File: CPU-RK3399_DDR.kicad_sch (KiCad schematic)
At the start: 29 parts, among them U1 RK3399

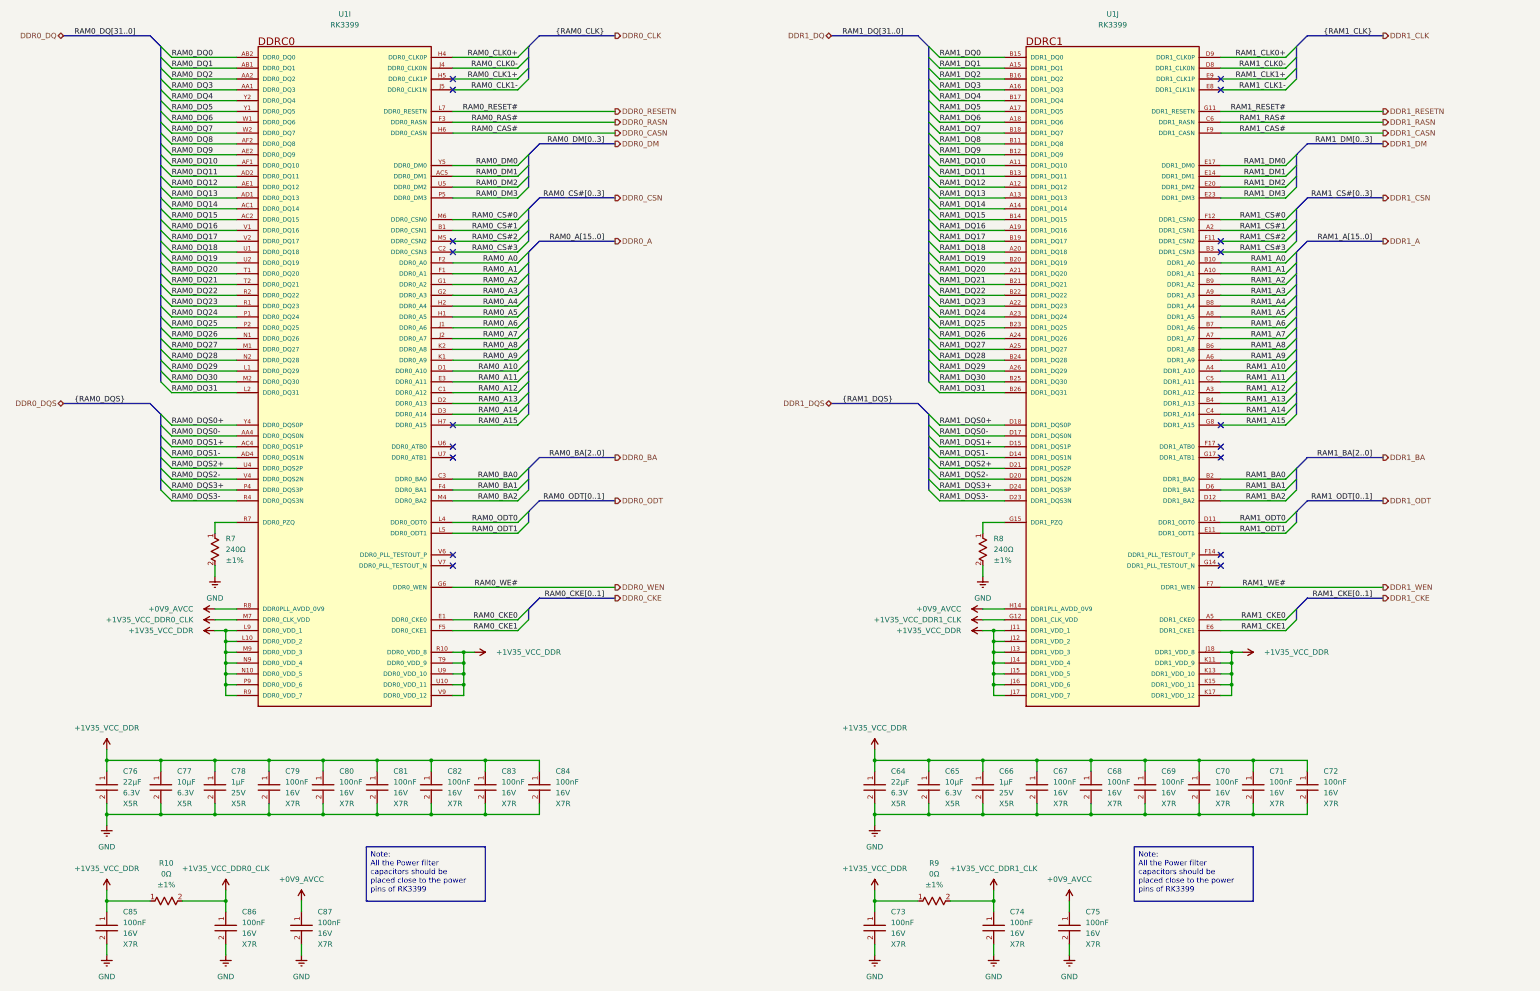
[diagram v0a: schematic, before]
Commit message: design CPU-RK3399 eMMC Controller
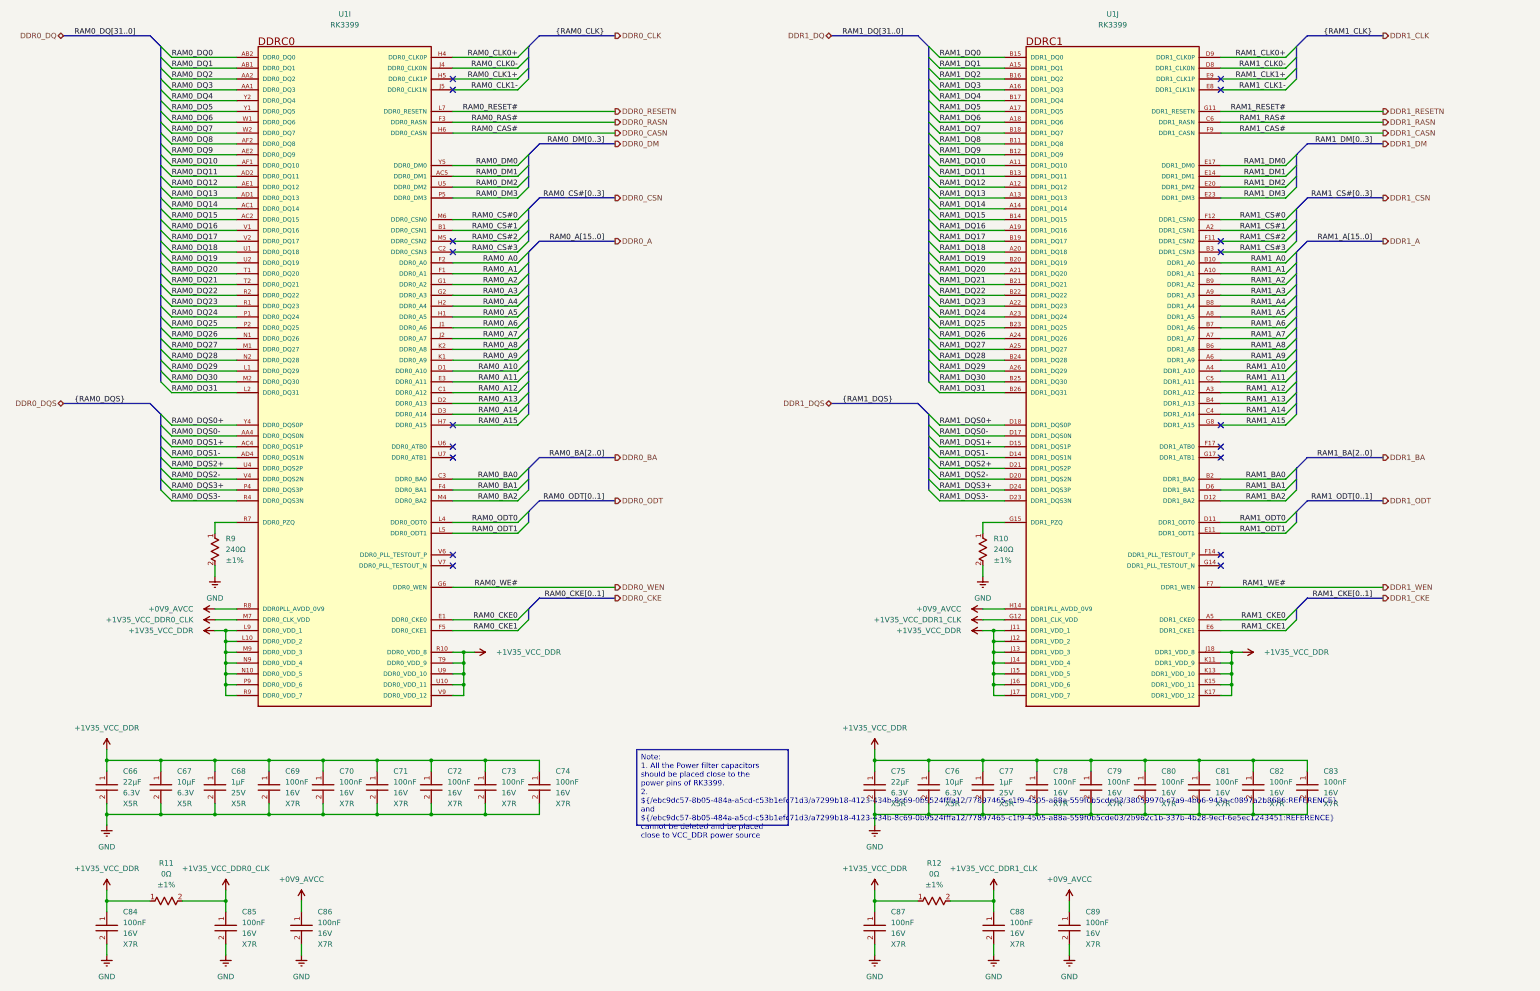
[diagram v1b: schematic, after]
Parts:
- renumbered C76 to C66, C77 to C67, C78 to C68, C79 to C69, C80 to C70, C81 to C71, C82 to C72, C83 to C73, C84 to C74, C64 to C75, C65 to C76, C66 to C77, C67 to C78, C68 to C79, C69 to C80, C70 to C81, C71 to C82, C72 to C83, C85 to C84, C86 to C85, C87 to C86, C73 to C87, C74 to C88, C75 to C89, R8 to R10, R10 to R11, R9 to R12, R7 to R9
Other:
- company: (none) -> TickLab
- title: (none) -> CPU-RK3399 DDR Controller

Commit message: design USB
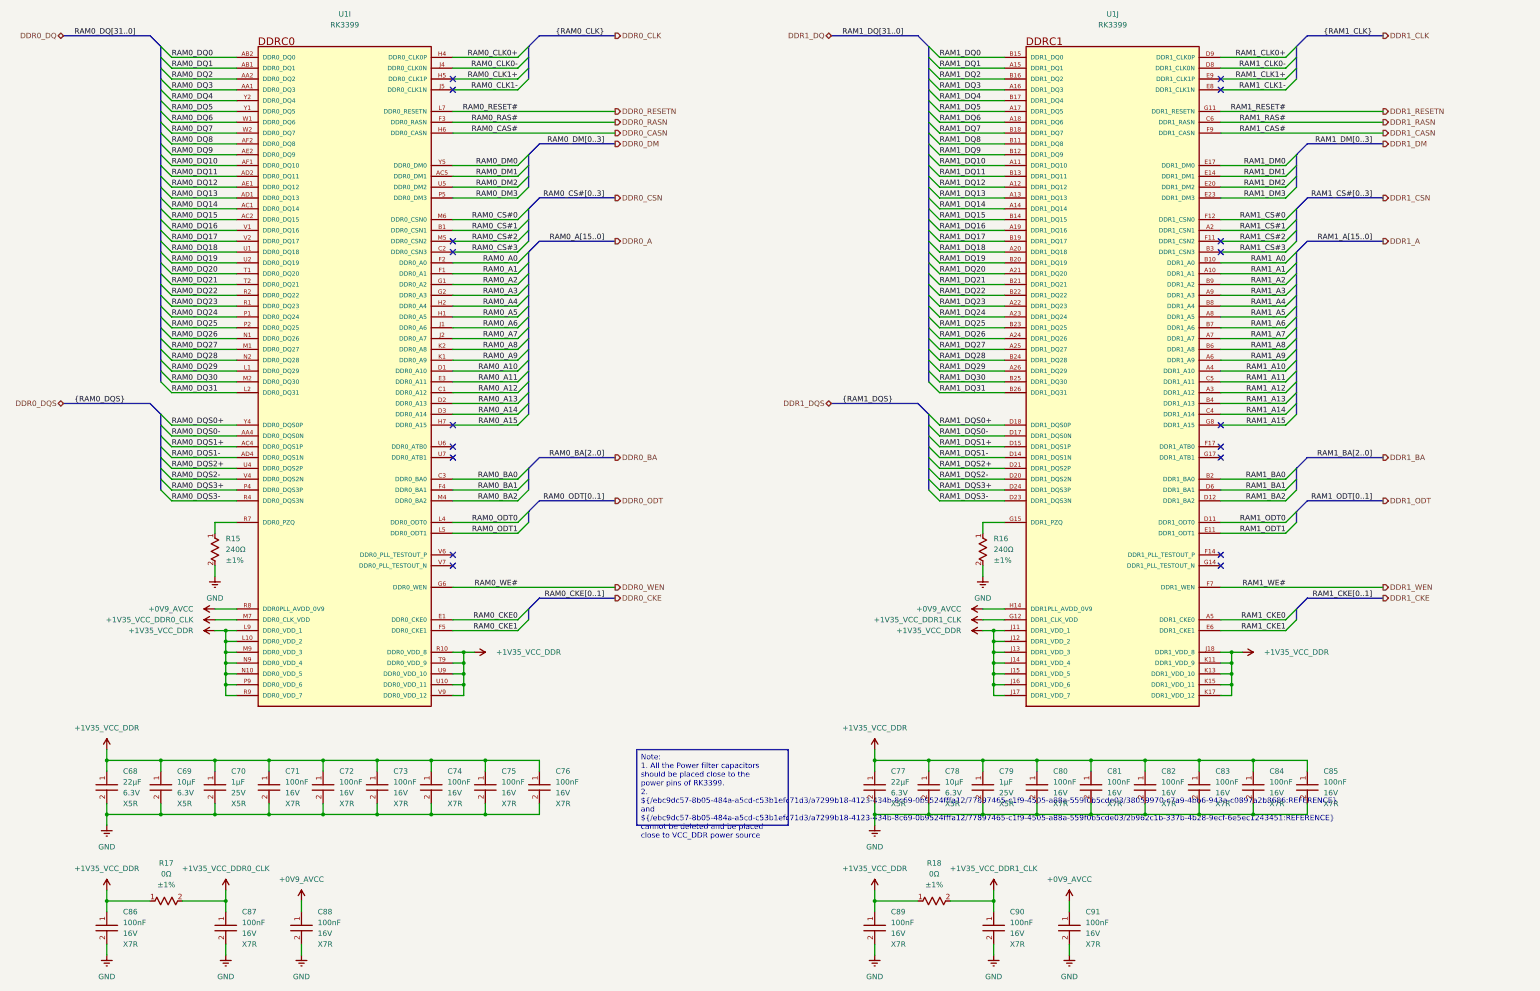
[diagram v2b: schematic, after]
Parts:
- renumbered C66 to C68, C67 to C69, C68 to C70, C69 to C71, C70 to C72, C71 to C73, C72 to C74, C73 to C75, C74 to C76, C75 to C77, C76 to C78, C77 to C79, C78 to C80, C79 to C81, C80 to C82, C81 to C83, C82 to C84, C83 to C85, C84 to C86, C85 to C87, C86 to C88, C87 to C89, C88 to C90, C89 to C91, R9 to R15, R10 to R16, R11 to R17, R12 to R18

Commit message: update design power
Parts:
- renumbered C68 to C123, C69 to C124, C70 to C125, C71 to C126, C72 to C127, C73 to C128, C74 to C129, C75 to C130, C76 to C131, C77 to C132, C78 to C133, C79 to C134, C80 to C135, C81 to C136, C82 to C137, C83 to C138, C84 to C139, C85 to C140, C86 to C141, C87 to C142, C88 to C143, C89 to C144, C90 to C145, C91 to C146, R15 to R38, R16 to R39, R17 to R40, R18 to R41, U1 to U2

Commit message: design DDR
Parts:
- renumbered C123 to C250, C124 to C251, C125 to C252, C126 to C253, C127 to C254, C128 to C255, C129 to C256, C130 to C257, C131 to C258, C132 to C259, C133 to C260, C134 to C261, C135 to C262, C136 to C263, C137 to C264, C138 to C265, C139 to C266, C140 to C267, C141 to C268, C142 to C269, C143 to C270, C144 to C271, C145 to C272, C146 to C273, R38 to R109, R39 to R110, R40 to R111, R41 to R112, U2 to U17
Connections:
- no-connect marks 18 -> 16
